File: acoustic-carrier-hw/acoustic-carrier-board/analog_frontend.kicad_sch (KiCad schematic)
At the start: 34 parts, among them IC1 ECP5-BGA256, J1 8P8C_Shielded, J8 Conn_02x04_Odd_Even, U3 MS9280

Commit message: [carrier] Added second adc input with magnetics, added ethernet connector with magnetics [piezodriver] Added diodes to level shifters for gate charge return current
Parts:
- removed R17: 0 +-1%, Resistor_SMD:R_0805_2012Metric_Pad1.20x1.40mm_HandSolder, symbol Device:R_Small
- added R50, R66, R69: 0 +-1%, Resistor_SMD:R_0805_2012Metric_Pad1.20x1.40mm_HandSolder, symbol Device:R_Small
- added R67, R68: 50 +- 1 %, Capacitor_SMD:C_0603_1608Metric_Pad1.08x0.95mm_HandSolder, symbol Device:R_Small
- added R71, R72, R73, R74: 1k, Resistor_SMD:R_0402_1005Metric, symbol Device:R_Small
- added RJ1: HR913550A, rj45:RJ45-TH_HR913550A, symbol RJ45_HR913550A:HR913550A
- R15, R16: value 50 +- 1 % -> 0 +-1%; footprint Capacitor_SMD:C_0603_1608Metric_Pad1.08x0.95mm_HandSolder -> Resistor_SMD:R_0805_2012Metric_Pad1.20x1.40mm_HandSolder; LPN 0603WAF510JT5E -> 0805W8F0000T5E; MPN C23197 -> C17477
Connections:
- net ADC_AIN1: now also R69.2
- net ADC_REFTS: now also R16.2, R66.2, R68.2; no longer C31.2, R15.2
- net ADC_VDDA_2: now also R67.2, R68.1, RJ1.4; no longer R15.1, R16.2
- net GND: now also R72.1, R73.2, RJ1.13, RJ1.14, RJ1.8 (GND)
- net VCORE_3V3: now also RJ1.12, RJ1.9
- net at C30.2: now also R50.1; no longer R16.1
- net ADC_LED_1: now reaches IC1.A5 (PT18A)
- net ADC_LED_1: now also R71.2, R72.2
- net ADC_LED_2: now reaches IC1.A6 (PT18B)
- net ADC_LED_2: now also R73.1, R74.2
- new net: C31.2, R66.1
- new net: R71.1, RJ1.11
- new net: R15.1, RJ1.1
- new net: R16.1, RJ1.2
- new net: R74.1, RJ1.10
- new net ADC_AIN1_RJ45: R15.2, R50.2, R67.1, R69.1
- no-connect marks 6 -> 10
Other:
- note added: "- Ethernet magnetics by default for decoupling - 0 ohm resistor in series for LC damping purposes (single-ended use) - Alternative input with DC-blocking capacitors with RJ45 Layout of transition between 2 ADC-inputs: - Use 0-ohm resistor to cross lower trace (instead of jumpers for signal integrity) Make sure the 0-ohm resistors and jumpers come together at the same spot LEDS: - Current through 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"
- note added: "ADC"
- note added: "ADC FRONTENDS"
- note added: "TODO: - Add extra BOOST/SEPIC-enable signals to connector"
- note removed: "- Differential impedance: 100 ohms - Input capacitance: 300 nF, f_plateau = 1/[2*pi*C*(R_diff/2)] = 30 kHz Max offst: 4% <<<< 1´ @ 1 MHz - Added 0-ohm series resistor in case of single-ended operation (LC damping)"
- note removed: "ADC FRONTEND"
- note removed: "TODO: - Think of reusing the same capacitive array twice - (once here once in the ethernet connection) - Think about buying some higher-rated C0G aprt instead of the capacitors - You'll need to add magnetics, c0G capacitors of that side = $$$ - Add extra BOOST/SEPIC-enable signals to connector"
- moved on the sheet: C30, C31, IC1B, J1, J8

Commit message: [piezodriver] Added temperature sensors + ldo + 8x2 connectors to carrier board
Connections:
- net FPGA_PWM_0: now also IC1.C6 (PT22A)
- net FPGA_PWM_1: now also IC1.B6 (PT22B)
- net FPGA_PWM_2: now also IC1.E7 (PT24A/GR_PCLK0_1)
- net FPGA_PWM_3: now also IC1.D7 (PT24B/GR_PCLK0_0)
- net BOOST_40V_EN: now reaches IC1.D6 (PT20B)
- net SEPIC_10V_EN: now reaches IC1.E6 (PT20A)
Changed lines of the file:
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@@
 		)
 	)
-	(text "- Ethernet magnetics by default for decoupling\n- 0 ohm resistor in series for LC damping purposes (single-ended use)\n- Alternative input with DC-blocking capacitors with RJ45\nLayout of transition between 2 ADC-inputs:\n- Use 0-ohm resistor to cross lower trace (instead of jumpers for signal integrity)\nMake sure the 0-ohm resistors and jumpers come together at the same spot\nLEDS:\n- Current through leds (3.3 - 2.2) / 2e3 = 0.55 mA (voltage drop 1.8-2.8 V)\n- Differential impedance: 100 ohms\n- Input capacitance: 300 nF, f_plateau = 1/[2*pi*C*(R_diff/2)] = 30 kHz\nMax offst: 4% <<<< 1' @ 1 MHz\n- Added 0-ohm series resistor in case of single-ended operation (LC damping)\nPin 13, 14: shield / frame connection"
+	(text "- Ethernet magnetics by default for decoupling\n- 0 ohm resistor in series for LC damping purposes (single-ended use)\n- Alternative input with DC-blocking capacitors with RJ45\nLayout of transition between 2 ADC-inputs:\n- Use 0-ohm resistor to cross lower trace (instead of jumpers for signal integrity)\nMake sure the 0-ohm resistors and jumpers come together at the same spot\nLEDS:\n- Current through leds (3.3 - 2.2) / 2e3 = 0.55 mA (voltage drop 1.8-2.8 V)\n- Differential impedance: 100 ohms\n- Input capacitance: 300 nF, f_plateau = 1/[2*pi*C*(R_diff/2)] = 30 kHz\nMax offst: 4% <<<< 1' @ 1 MHz\n- Added 0-ohm series resistor in case of single-ended operation (LC damping)\nPin 13, 14: shield / frame connection\nGround\n- Chassis ground vs signal ground connection"
 		(exclude_from_sim no)
 		(at 299.974 41.656 0)
@@
 	(text "TODO:\n- Add extra BOOST/SEPIC-enable signals to connector"
 		(exclude_from_sim no)
-		(at -33.02 40.64 0)
+		(at -63.754 46.228 0)
 		(effects
 			(font
@@
 	(wire
 		(pts
+			(xy 90.17 72.39) (xy 95.25 72.39)
+		)
+		(stroke
+			(width 0)
+			(type default)
+		)
+	)
+	(wire
+		(pts
 			(xy 250.19 66.04) (xy 254 66.04)
 		)
@@
 	(wire
 		(pts
+			(xy 90.17 74.93) (xy 95.25 74.93)
+		)
+		(stroke
+			(width 0)
+			(type default)
+		)
+	)
+	(wire
+		(pts
 			(xy 29.21 180.34) (xy 29.21 181.61)
 		)
@@
 	(wire
 		(pts
+			(xy 90.17 69.85) (xy 95.25 69.85)
+		)
+		(stroke
+			(width 0)
+			(type default)
+		)
+	)
+	(wire
+		(pts
 			(xy 255.27 43.18) (xy 255.27 50.8)
 		)
@@
 	(wire
 		(pts
+			(xy 90.17 82.55) (xy 95.25 82.55)
+		)
+		(stroke
+			(width 0)
+			(type default)
+		)
+	)
+	(wire
+		(pts
 			(xy 40.64 160.02) (xy 39.37 160.02)
 		)
@@
 	(wire
 		(pts
+			(xy 90.17 80.01) (xy 95.25 80.01)
+		)
+		(stroke
+			(width 0)
+			(type default)
+		)
+	)
+	(wire
+		(pts
 			(xy 25.4 160.02) (xy 31.75 160.02)
 		)
@@
 		(pts
 			(xy 83.82 166.37) (xy 83.82 167.64)
+		)
+		(stroke
+			(width 0)
+			(type default)
+		)
+	)
+	(wire
+		(pts
+			(xy 90.17 77.47) (xy 95.25 77.47)
 		)
 		(stroke
@@
 		)
 	)
+	(global_label "SEPIC_10V_EN"
+		(shape output)
+		(at 90.17 69.85 180)
+		(fields_autoplaced yes)
+		(effects
+			(font
+				(size 1.27 1.27)
+			)
+			(justify right)
+		)
+		(property "Intersheetrefs" "${INTERSHEET_REFS}"
+			(at 73.7592 69.85 0)
+			(effects
+				(font
+					(size 1.27 1.27)
+				)
+				(justify right)
+				(hide yes)
+			)
+		)
+	)
+	(global_label "FPGA_PWM_0"
+		(shape output)
+		(at 90.17 74.93 180)
+		(fields_autoplaced yes)
+		(effects
+			(font
+				(size 1.27 1.27)
+			)
+			(justify right)
+		)
+		(property "Intersheetrefs" "${INTERSHEET_REFS}"
+			(at 75.1501 74.93 0)
+			(effects
+				(font
+					(size 1.27 1.27)
+				)
+				(justify right)
+				(hide yes)
+			)
+		)
+	)
+	(global_label "BOOST_40V_EN"
+		(shape output)
+		(at 90.17 72.39 180)
+		(fields_autoplaced yes)
+		(effects
+			(font
+				(size 1.27 1.27)
+			)
+			(justify right)
+		)
+		(property "Intersheetrefs" "${INTERSHEET_REFS}"
+			(at 73.1544 72.39 0)
+			(effects
+				(font
+					(size 1.27 1.27)
+				)
+				(justify right)
+				(hide yes)
+			)
+		)
+	)
+	(global_label "FPGA_PWM_2"
+		(shape output)
+		(at 90.17 80.01 180)
+		(fields_autoplaced yes)
+		(effects
+			(font
+				(size 1.27 1.27)
+			)
+			(justify right)
+		)
+		(property "Intersheetrefs" "${INTERSHEET_REFS}"
+			(at 75.1501 80.01 0)
+			(effects
+				(font
+					(size 1.27 1.27)
+				)
+				(justify right)
+				(hide yes)
+			)
+		)
+	)
 	(global_label "FPGA_PWM_1"
 		(shape input)
@@
 				(hide yes)
 			)
+		)
+	)
+	(global_label "FPGA_PWM_1"
+		(shape output)
+		(at 90.17 77.47 180)
+		(fields_autoplaced yes)
+		(effects
+			(font
+				(size 1.27 1.27)
+			)
+			(justify right)
+		)
+		(property "Intersheetrefs" "${INTERSHEET_REFS}"
+			(at 75.1501 77.47 0)
+			(effects
+				(font
+					(size 1.27 1.27)
+				)
+				(justify right)
+				(hide yes)
+			)
+		)
+	)
+	(global_label "FPGA_PWM_3"
+		(shape output)
+		(at 90.17 82.55 180)
+		(fields_autoplaced yes)
+		(effects
+			(font
+				(size 1.27 1.27)
+			)
+			(justify right)
+		)
+		(property "Intersheetrefs" "${INTERSHEET_REFS}"
+			(at 75.1501 82.55 0)
+			(effects
+				(font
+					(size 1.27 1.27)
+				)
+				(justify right)
+				(hide yes)
+			)

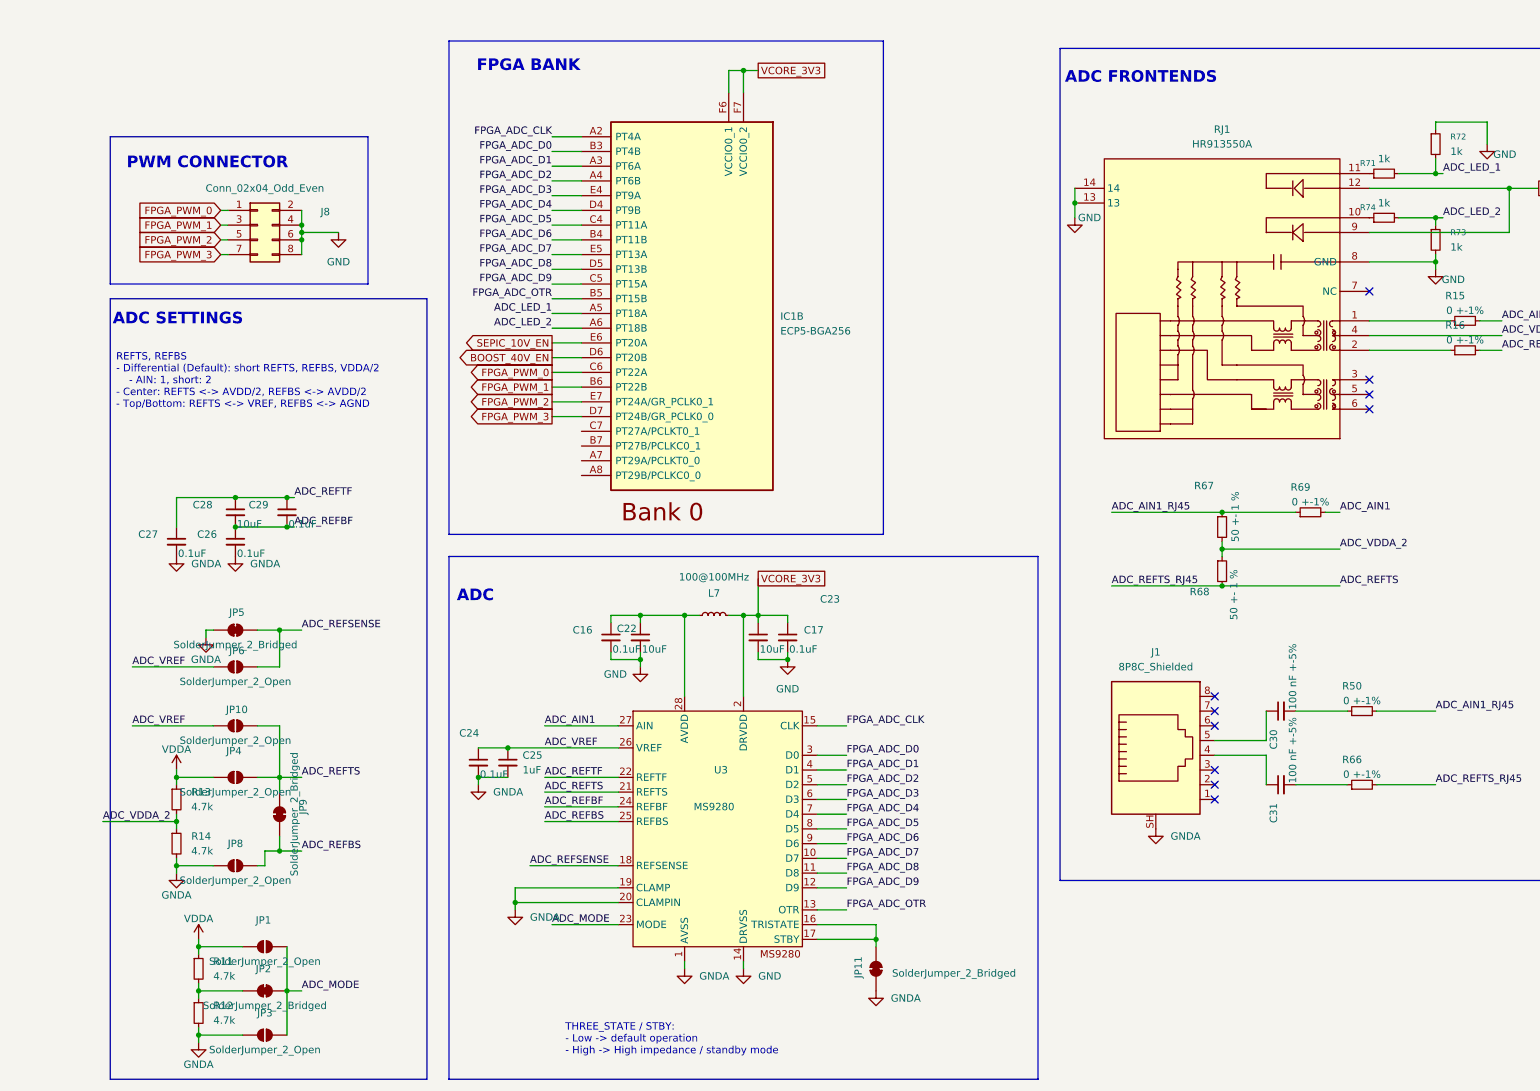
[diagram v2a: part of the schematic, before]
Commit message: [carrier] Started schematic check, replaced 8 with 16 pin connectors
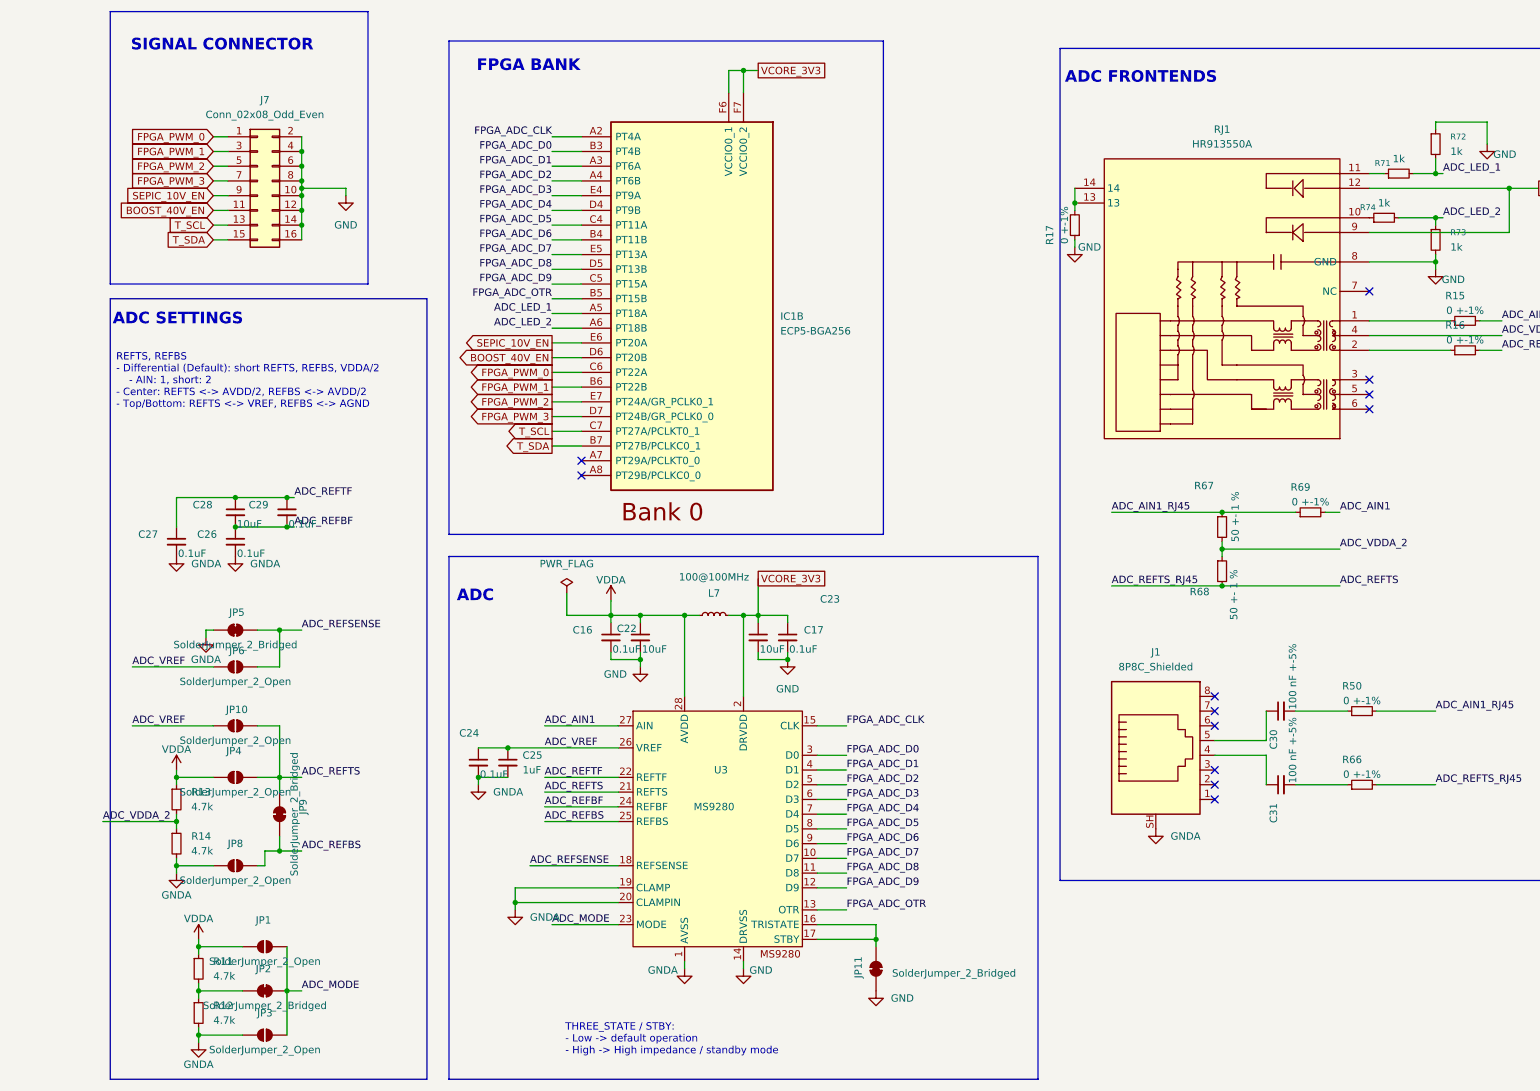
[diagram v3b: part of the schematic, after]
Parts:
- removed J8: Conn_02x04_Odd_Even, Connector_PinSocket_2.54mm:PinSocket_2x04_P2.54mm_Horizontal, symbol Connector_Generic:Conn_02x04_Odd_Even
- added J7: Conn_02x08_Odd_Even, Connector_PinSocket_2.54mm:PinSocket_2x08_P2.54mm_Horizontal, symbol Connector_Generic:Conn_02x08_Odd_Even
- added R17: 0 +-1%, Resistor_SMD:R_0805_2012Metric_Pad1.20x1.40mm_HandSolder, symbol Device:R_Small
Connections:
- net BOOST_40V_EN: now also J7.11 (Pin_11)
- net FPGA_PWM_0: now also J7.1 (Pin_1)
- net FPGA_PWM_1: now also J7.3 (Pin_3)
- net FPGA_PWM_2: now also J7.5 (Pin_5)
- net FPGA_PWM_3: now also J7.7 (Pin_7)
- net GND: now also JP11.1 (A), J7.10 (Pin_10), J7.12 (Pin_12), J7.14 (Pin_14), J7.16 (Pin_16), J7.2 (Pin_2), J7.4 (Pin_4), J7.6 (Pin_6), J7.8 (Pin_8), R17.1; no longer RJ1.13, RJ1.14
- net GNDA: no longer JP11.1 (A)
- net SEPIC_10V_EN: now also J7.9 (Pin_9)
- net VDDA: now also C16.1, C22.1, L7.2, U3.28 (AVDD)
- net T_SDA: now reaches IC1.B7 (PT27B/PCLKC0_1)
- net T_SDA: now also J7.15 (Pin_15)
- net T_SCL: now reaches IC1.C7 (PT27A/PCLKT0_1)
- net T_SCL: now also J7.13 (Pin_13)
- new net: R17.2, RJ1.13, RJ1.14
- no-connect marks 10 -> 12
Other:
- note added: "SIGNAL CONNECTOR"
- note removed: "PWM CONNECTOR"
- moved on the sheet: R71

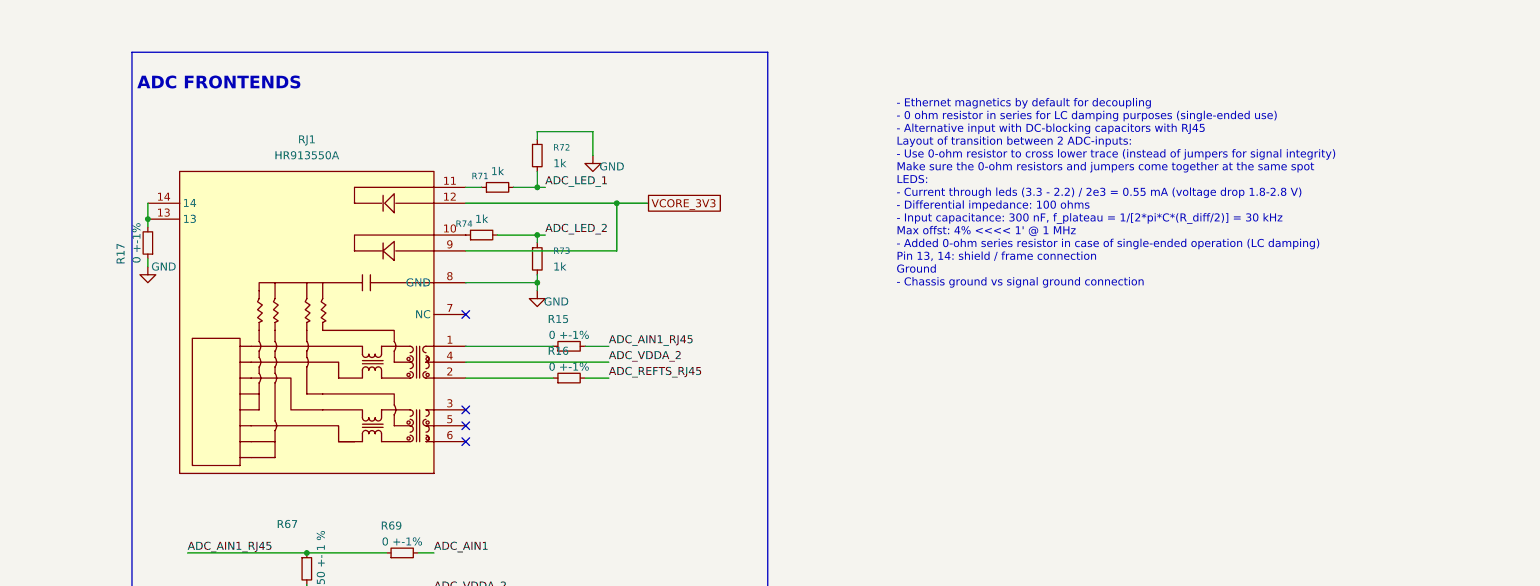
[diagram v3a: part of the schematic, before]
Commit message: [carrier] removed external led, using ethernet leds, replaced 1kOhm by 470 ohm resistors
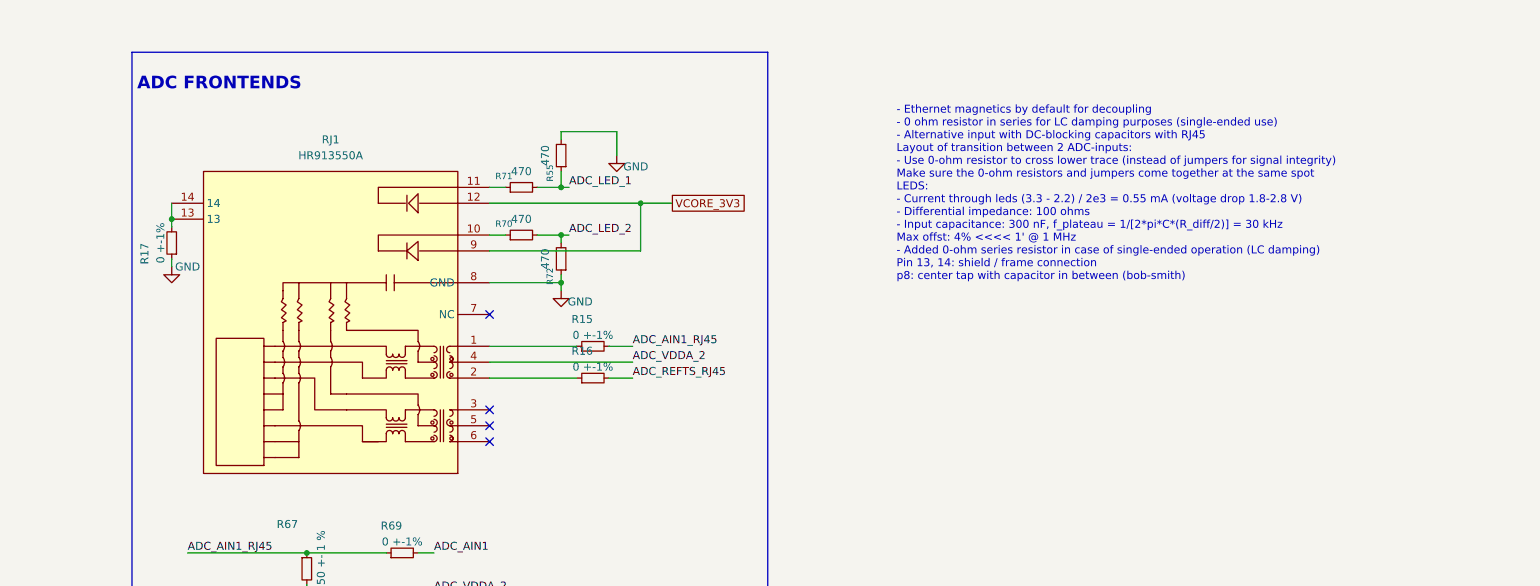
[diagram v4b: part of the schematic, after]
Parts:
- removed R73, R74: 1k, Resistor_SMD:R_0402_1005Metric, symbol Device:R_Small
- added R55, R70: 470, Resistor_SMD:R_0603_1608Metric, symbol Device:R_Small
- R71, R72: value 1k -> 470; footprint Resistor_SMD:R_0402_1005Metric -> Resistor_SMD:R_0603_1608Metric; LPN C11702 -> C23179; MPN 0402WGF1001TCE -> 0603WAF4700T5E
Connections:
- net ADC_LED_1: now also R55.1; no longer R72.2
- net ADC_LED_2: now also R72.2, R70.2
- net GND: now also R55.2
- net at RJ1.10: now also R70.1
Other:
- moved on the sheet: R15, R16, R17, R71, RJ1

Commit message: [carrier] Fixed most of the carrier board ERC issues (next) fix BGA ERC issue
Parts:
- IC1: footprint BGA256C80P16X16_1400X1400X170 -> fpga:BGA256C80P16X16_1400X1400X170; LPN (none) -> C1521614; MPN (none) -> LFE5U-25F-6BG256C; Part Number LFE5U-12F-6BG256C -> LFE5U-25F-6BG256C
- RJ1: LCSC Part (none) -> C163507
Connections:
- net GNDA is gone; now on net GND: C24.2, C25.2, C26.2, C27.2, J1.SH, JP3.1 (A), JP5.1 (A), JP8.1 (A), R12.2, R14.2, U3.1 (AVSS), U3.19 (CLAMP), U3.20 (CLAMPIN)

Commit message: [carrier] Fixed ERC errors and fpga-footprints (next) ) add extra pin functionality to 2 remaining banks, perform schematic checks
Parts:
- removed JP11: SolderJumper_2_Bridged, symbol Jumper:SolderJumper_2_Bridged
- removed R68: 50 +- 1 %, Capacitor_SMD:C_0603_1608Metric_Pad1.08x0.95mm_HandSolder, symbol Device:R_Small
- added JP7: SolderJumper_2_Bridged, Jumper:SolderJumper-2_P1.3mm_Bridged_Pad1.0x1.5mm, symbol Jumper:SolderJumper_2_Bridged
- added R24: 51 +- 1 %, Resistor_SMD:R_0603_1608Metric_Pad0.98x0.95mm_HandSolder, symbol Device:R_Small
- IC1: Part Number LFE5U-25F-6BG256C -> (none)
- JP1, JP10, JP3, JP4, JP6, JP8: footprint Jumper:SolderJumper-3_P1.3mm_Bridged12_Pad1.0x1.5mm_NumberLabels -> Jumper:SolderJumper-2_P1.3mm_Open_Pad1.0x1.5mm
- JP2, JP5, JP9: footprint (none) -> Jumper:SolderJumper-2_P1.3mm_Bridged_Pad1.0x1.5mm
- R67: value 50 +- 1 % -> 51 +- 1 %; footprint Capacitor_SMD:C_0603_1608Metric_Pad1.08x0.95mm_HandSolder -> Resistor_SMD:R_0603_1608Metric_Pad0.98x0.95mm_HandSolder
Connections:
- net ADC_REFBS: now also JP7.1 (A); no longer JP9.1 (A)
- net ADC_REFTS: now also JP7.2 (B), R24.2; no longer JP9.2 (B)
- net ADC_VDDA_2: now also R24.1
- net GND: now also JP9.1 (A)
- net at U3.16 (TRISTATE), U3.17 (STBY): now also JP9.2 (B)
